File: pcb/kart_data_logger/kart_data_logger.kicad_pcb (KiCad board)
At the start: 2 copper layers, 19 parts, among them J1 GPS, J2 I2S AMP, J3 Battery, Q1 BC327, Q2 2N3904, Q3 2N3904, U2 XIAO-ESP32-S3-SMD

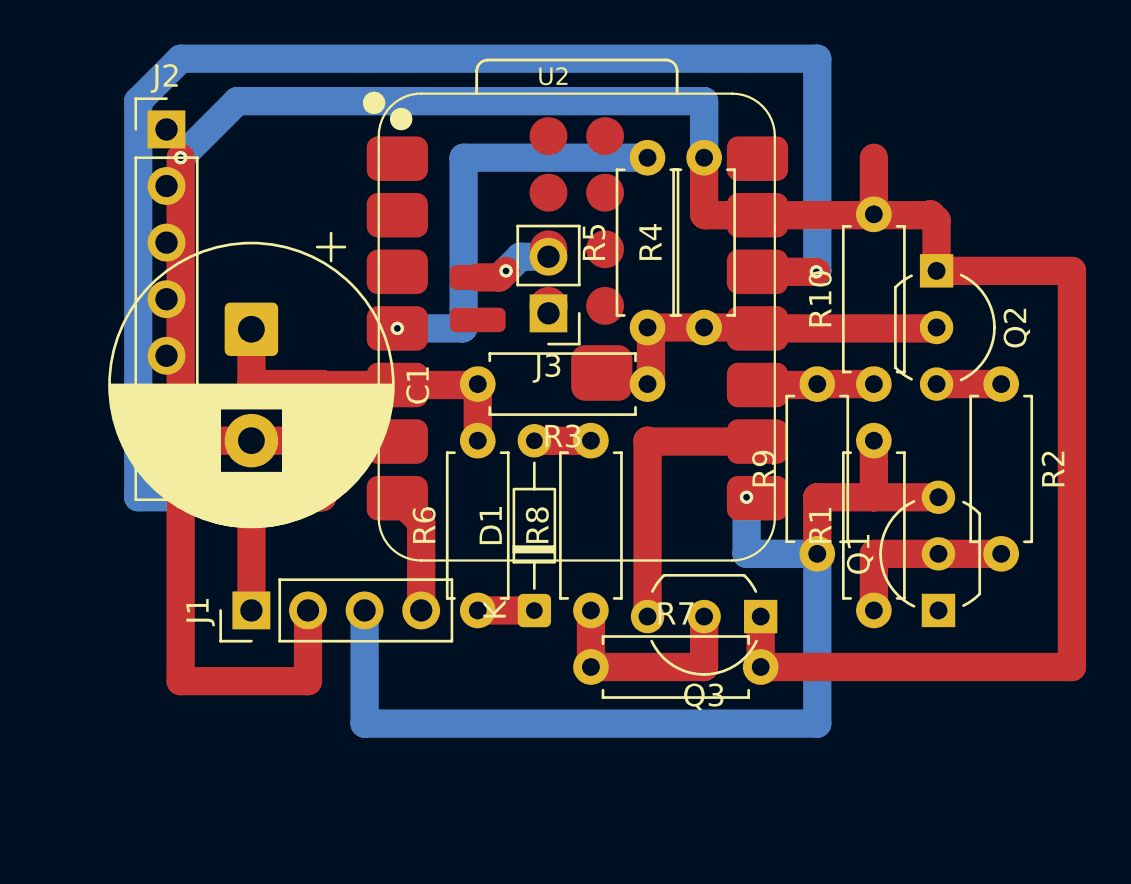
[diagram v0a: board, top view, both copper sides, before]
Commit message: updated KiCad project files; updated platformio.ini to change upload port and include MPU6050 library for IMU support; modified main_display.cpp to integrate IMU data handling and adjust telemetry based on GPS provider; refactored main_logger.cpp to streamline IMU data retrieval and telemetry message construction; improved initialization sequence for IMU and display components in setup functions;
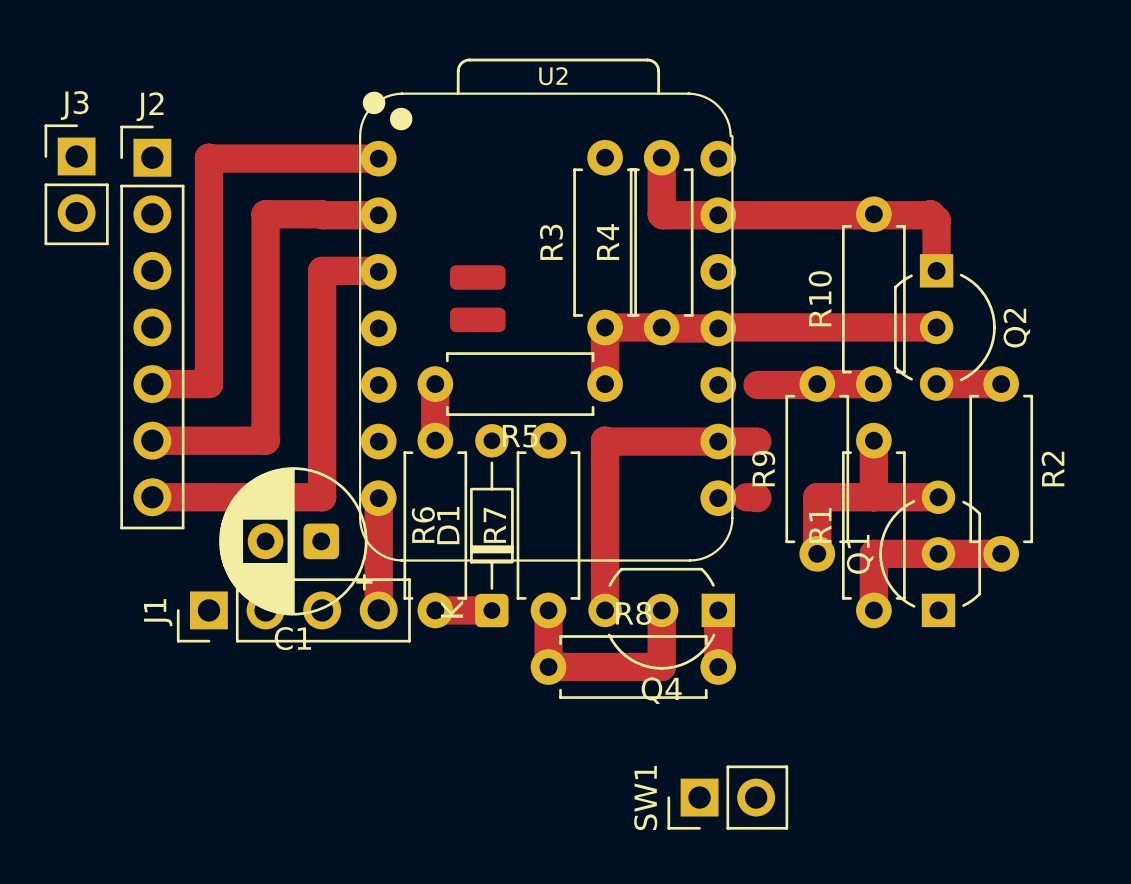
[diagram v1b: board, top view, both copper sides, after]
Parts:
- added SW1: ON/OFF, Connector_PinHeader_2.54mm:PinHeader_1x02_P2.54mm_Vertical, F.Cu at (177.0, 110.0)
- C1: footprint Capacitor_THT:CP_Radial_D12.5mm_P5.00mm -> Capacitor_THT:CP_Radial_D6.3mm_P2.50mm
- R3: renamed from R5; value R -> 1k
- moved J3 22.3 mm to (149.0, 81.2), turned to 0 degrees
- moved C1 10.0 mm to (160.0, 98.5), turned to 180 degrees
- moved Q4 1.92 mm to (177.8, 101.6)
- moved D1 1.91 mm to (167.6, 101.6)
- moved J1 1.91 mm to (154.9, 101.6)
- moved R3 1.91 mm to (172.7, 88.9)
- moved R4 1.91 mm to (175.3, 88.9)
- moved R5 1.91 mm to (172.7, 91.4)
- moved R6 1.91 mm to (165.1, 101.6)
- moved R7 1.91 mm to (170.2, 101.6)
- moved R8 1.91 mm to (170.2, 104.1)
- moved J2 1.42 mm to (152.4, 81.3)
- renumbered Q3 to Q4, R3 to R5, R8 to R7, R7 to R8
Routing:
- net GND: track 127.4 -> 19.8 mm, vias 2 -> 0
- net +3.3V: track 77.8 -> 0.00 mm, vias 1 -> 0
- net Net-(J1-Pin_3): track 39.2 -> 0.51 mm, vias 1 -> 0
- net Net-(J2-Pin_6): track 0.00 -> 20.3 mm
- net Net-(J2-Pin_7): track 0.00 -> 20.3 mm
- net /D3: track 18.9 -> 0.00 mm, vias 1 -> 0
- net Net-(J2-Pin_5): track 15.2 -> 20.5 mm
- net Net-(D1-A): track 2.54 -> 0.00 mm
- net Net-(C1-Pad1): track 0.00 -> 2.54 mm
- net /jump: track 15.6 -> 17.5 mm
- net /D8: track 12.8 -> 14.5 mm
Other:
- copper layers 2 -> 12
